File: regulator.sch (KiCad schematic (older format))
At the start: 21 parts, among them IC1 PIC12F675-I/P, Q1 PN2222A, Q2 2N2907A, Q3 PHP18NQ10T, Q4 PN2222A, U1 LM7805

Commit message: Replace old circuit.
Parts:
- added D5: 1N4007, symbol D
- D2: value D -> 1N4004
- Q1, Q4: symbol Q_NPN_EBC -> Q_NPN_EBC-RESCUE-regulator
- Q2: symbol Q_PNP_EBC -> Q_PNP_EBC-RESCUE-regulator
- Q3: value PHP18NQ10T -> BUK9511-55A (Logic Level); symbol Q_NMOS_GDS -> Q_NMOS_GDS-RESCUE-regulator
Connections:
- net BootStrap: no longer U1.VI
- net Vin(14+): now also D5.2 (A); no longer D2.2 (A)
- net at C1.1, IC1.1 (VDD), U1.VO: now also D2.2 (A)
- new net: D5.1 (K), U1.VI
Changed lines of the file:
@@
 EESchema Schematic File Version 2
+LIBS:regulator-rescue
 LIBS:power
 LIBS:device
@@
 encoding utf-8
 Sheet 1 1
-Title "PWM Regulator v1"
-Date "2015'년' 05'월' 29'일' 금요일"
-Rev "1.2"
+Title "PWM Regulator v2"
+Date "2015-06-18"
+Rev "1.2c"
 Comp ""
 Comment1 ""
@@
 Connection ~ 8950 5000
 $Comp
-L Q_NMOS_GDS Q3
+L Q_NMOS_GDS-RESCUE-regulator Q3
 U 1 1 5563B1A2
 P 6600 3250
-F 0 "Q3" H 6900 3300 50  0000 R CNN
-F 1 "PHP18NQ10T" H 7250 3200 50  0000 R CNN
+F 0 "Q3" V 6850 3500 50  0000 R CNN
+F 1 "BUK9511-55A (Logic Level)" V 7000 3500 50  0000 R CNN
 F 2 "" H 6800 3350 29  0000 C CNN
 F 3 "" H 6600 3250 60  0000 C CNN
@@
 $EndComp
 $Comp
-L Q_NPN_EBC Q1
+L Q_NPN_EBC-RESCUE-regulator Q1
 U 1 1 5563BACB
 P 6200 3850
@@
 $EndComp
 $Comp
-L Q_PNP_EBC Q2
+L Q_PNP_EBC-RESCUE-regulator Q2
 U 1 1 5563BB02
 P 6200 4300
@@
 P 4900 3350
 F 0 "D2" H 4900 3450 50  0000 C CNN
-F 1 "D" H 4900 3250 50  0000 C CNN
+F 1 "1N4004" H 4900 3250 50  0000 C CNN
 F 2 "" H 4900 3350 60  0000 C CNN
 F 3 "" H 4900 3350 60  0000 C CNN
@@
 	4650 4150 5250 4150
 Wire Wire Line
-	4750 3350 4600 3350
-Wire Wire Line
-	4600 3350 4600 3150
-Wire Wire Line
 	5250 4150 5250 4400
 $Comp
-L Q_NPN_EBC Q4
+L Q_NPN_EBC-RESCUE-regulator Q4
 U 1 1 55642E1A
 P 5350 4050
@@
 Connection ~ 5450 3750
 Wire Wire Line
-	5450 4250 5450 5000
+	5450 5000 5450 4250
 Connection ~ 5450 5000
 Wire Wire Line
@@
 	2150 5000 9500 5000
 Wire Wire Line
-	2700 4300 2700 4050
+	2700 3350 2700 4300
 Connection ~ 2700 4050
 Wire Wire Line
@@
 $EndComp
 Wire Wire Line
-	7600 3150 7350 3150
-Wire Wire Line
-	7050 3150 6800 3150
-Wire Wire Line
-	5200 3350 5200 3600
-Wire Wire Line
-	5200 3600 1750 3600
-Connection ~ 5200 3350
-Wire Wire Line
-	1750 3600 1750 4050
-Wire Wire Line
-	4600 3150 6400 3150
+	7350 3150 7600 3150
+Wire Wire Line
+	6800 3150 7050 3150
+Wire Wire Line
+	1750 3150 1750 4050
 Text GLabel 2150 2800 0    60   Input ~ 0
 Vin(14+)
@@
 Vin-
 Wire Wire Line
-	2150 5050 1950 5050
+	2150 5050 1900 5050
 Connection ~ 2150 5000
 $Comp
@@
 	5050 4950 5050 5000
 Connection ~ 5050 5000
+Wire Wire Line
+	2700 3350 4750 3350
+Wire Wire Line
+	3500 3150 6400 3150
+$Comp
+L D D5
+U 1 1 558499A4
+P 3350 3150
+F 0 "D5" H 3350 3250 50  0000 C CNN
+F 1 "1N4007" H 3350 3050 50  0000 C CNN
+F 2 "" H 3350 3150 60  0000 C CNN
+F 3 "" H 3350 3150 60  0000 C CNN
+	1    3350 3150
+	1    0    0    1
+$EndComp
+Wire Wire Line
+	3200 3150 1750 3150
 $EndSCHEMATC

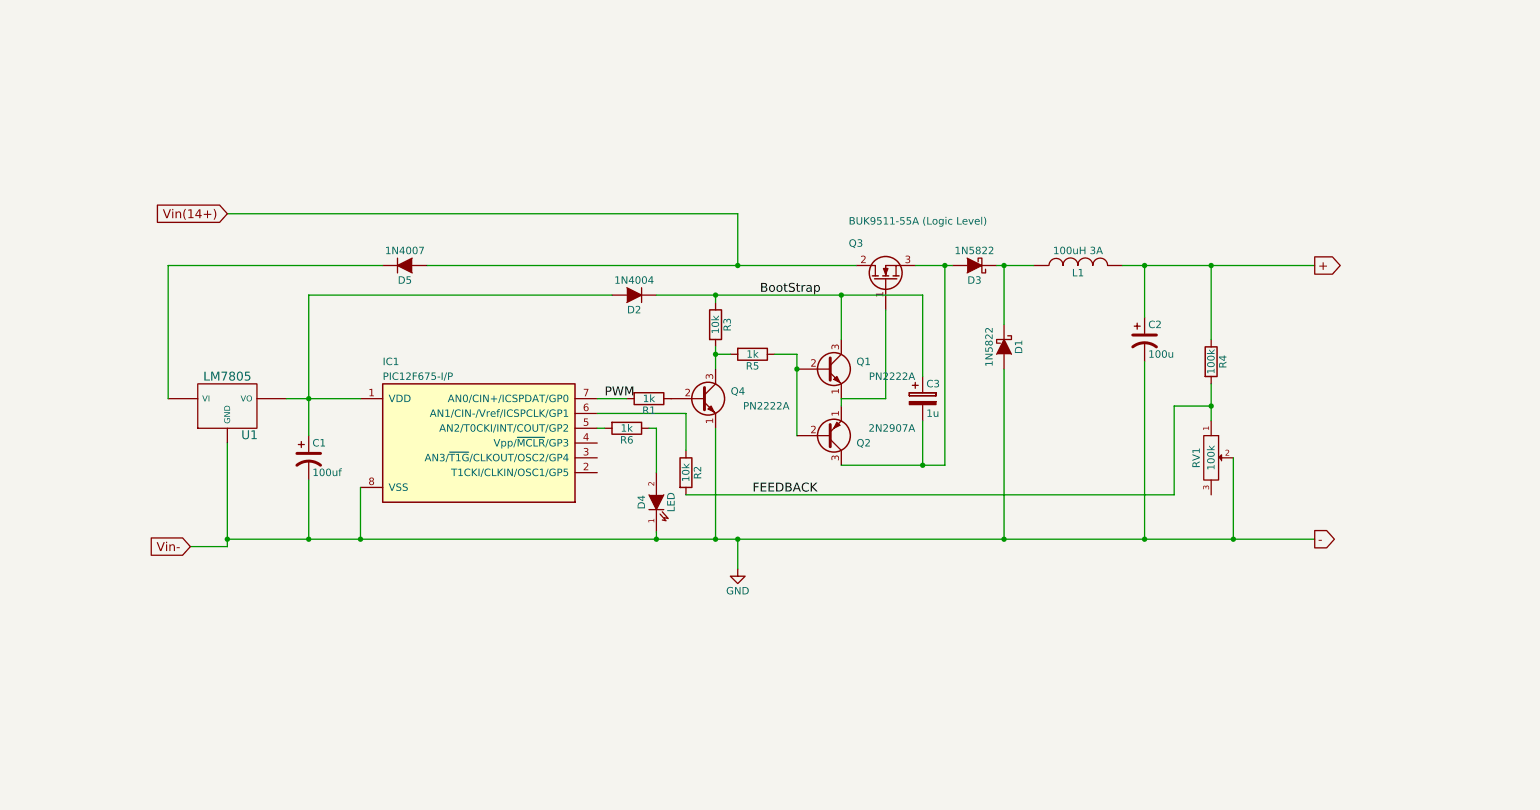
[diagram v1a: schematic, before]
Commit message: Add Solar Engine. It prevent drop PV voltage at low voltage load. It's not fully tested and some noise from switching.
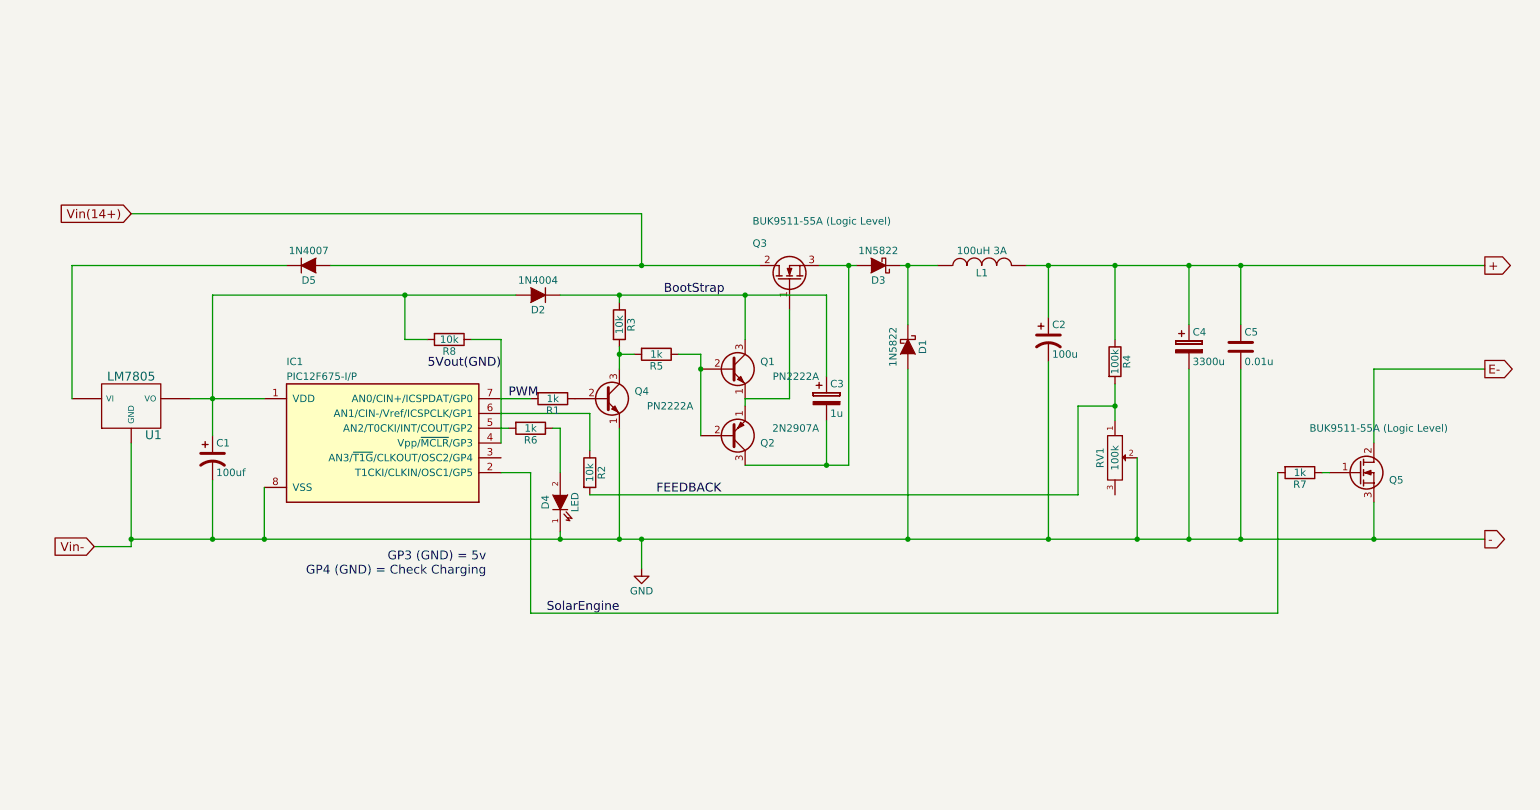
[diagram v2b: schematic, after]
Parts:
- added C4: 3300u, symbol CP
- added C5: 0.01u, symbol C
- added Q5: BUK9511-55A (Logic Level), symbol Q_NMOS_GDS-RESCUE-regulator
- added R7: 1k, symbol R
- added R8: 10k, symbol R
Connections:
- net +: now also C4.1, C5.1
- net GND: now also C4.2, C5.2, Q5.3 (S)
- net at C1.1, D2.2 (A), IC1.1 (VDD)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: now also R8.2
- net SolarEngine: now reaches IC1.2 (T1CKI/CLKIN/OSC1/GP5)
- net SolarEngine: now also R7.2
- net 5Vout(GND): now reaches IC1.4 (Vpp/~MCLR~/GP3)
- net 5Vout(GND): now also R8.1
- new net: Q5.1 (G), R7.1
- new net E-: Q5.2 (D)
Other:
- note added: "GP3 (GND) = 5v\nGP4 (GND) = Check Charging"
- moved on the sheet: C1, C2, C3, D1, D2, D3, D4, D5, IC1, L1, Q1, Q2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

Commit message: Solar Engine is not good idea but test works.
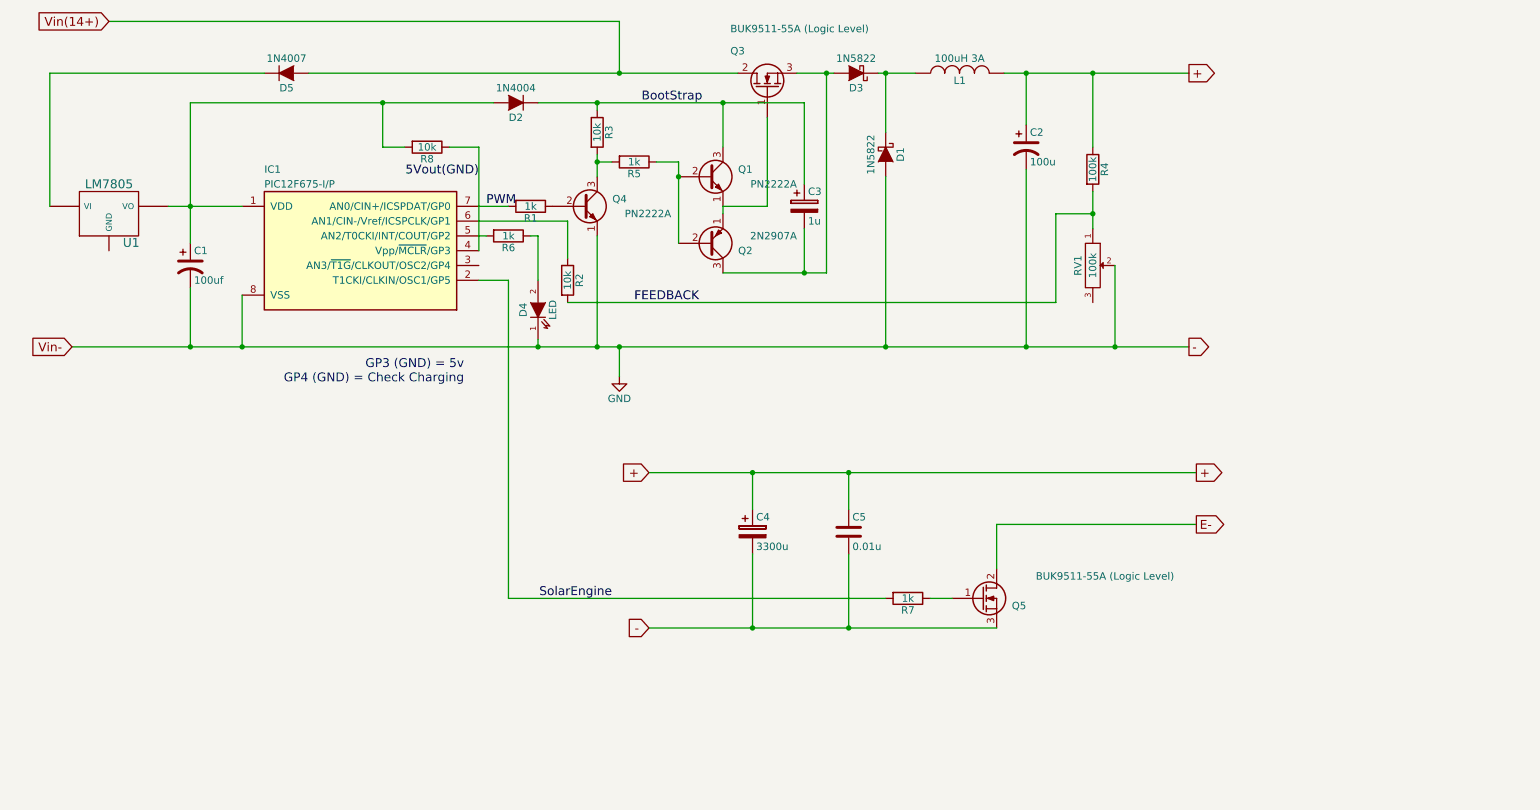
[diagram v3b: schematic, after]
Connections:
- net GND: no longer U1.GND
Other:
- moved on the sheet: C1, C2, C3, C4, C5, D1, D2, D3, D4, D5, IC1, L1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

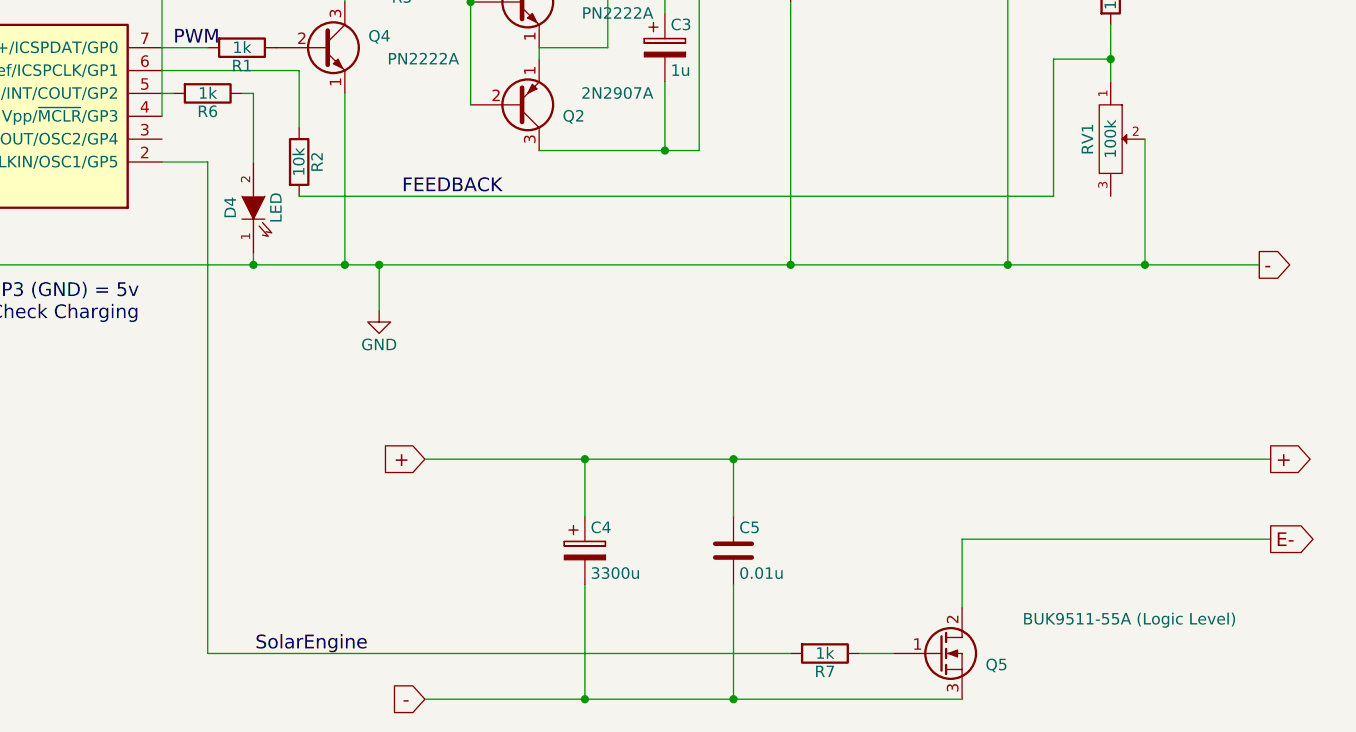
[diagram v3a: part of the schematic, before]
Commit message: Remove Solar Engine. It is useless. Add signal for PWM Sync.
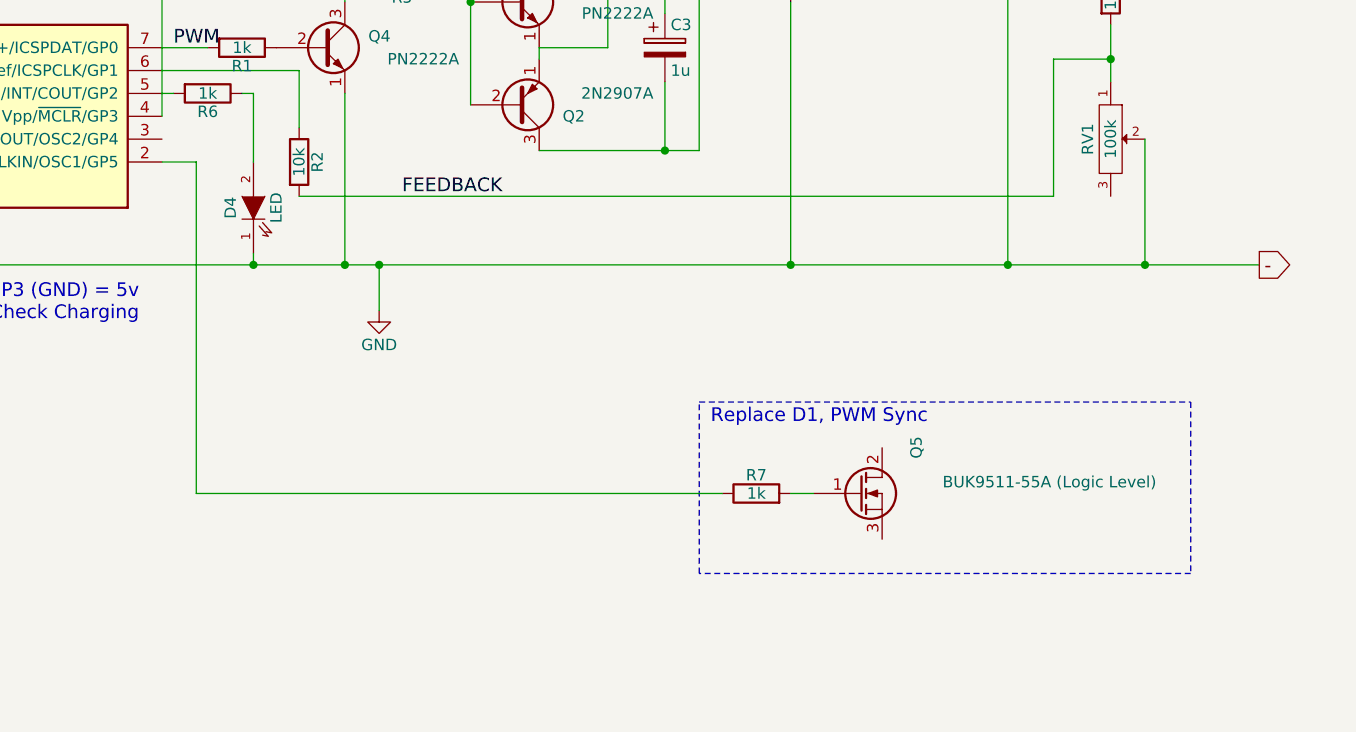
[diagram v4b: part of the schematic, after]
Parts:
- removed C4: 3300u, symbol CP
- removed C5: 0.01u, symbol C
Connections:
- net GND: no longer Q5.3 (S)
- net at R7.1: now also IC1.2 (T1CKI/CLKIN/OSC1/GP5); no longer Q5.1 (G)
- net E-: no longer names the net of Q5.2 (D)
- net SolarEngine: no longer names the net of R7.2
- net SolarEngine: now also Q5.1 (G); no longer IC1.2 (T1CKI/CLKIN/OSC1/GP5)
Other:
- note added: "Replace D1, PWM Sync"
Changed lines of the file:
@@
 Sheet 1 1
 Title "PWM Regulator v3"
-Date "2015-07-14"
-Rev "1.2f"
+Date "2015-07-18"
+Rev "1.2g"
 Comp ""
 Comment1 ""
@@
 $EndComp
 $Comp
-L CP C4
-U 1 1 559FC9C7
-P 5700 4950
-F 0 "C4" H 5725 5050 50  0000 L CNN
-F 1 "3300u" H 5725 4850 50  0000 L CNN
-F 2 "" H 5738 4800 30  0000 C CNN
-F 3 "" H 5700 4950 60  0000 C CNN
-	1    5700 4950
-	1    0    0    -1
-$EndComp
-$Comp
-L C C5
-U 1 1 559FCBD8
-P 6350 4950
-F 0 "C5" H 6375 5050 50  0000 L CNN
-F 1 "0.01u" H 6375 4850 50  0000 L CNN
-F 2 "" H 6388 4800 30  0000 C CNN
-F 3 "" H 6350 4950 60  0000 C CNN
-	1    6350 4950
-	1    0    0    -1
-$EndComp
-$Comp
-L Q_NMOS_GDS-RESCUE-regulator Q5
-U 1 1 559FCD3F
-P 7250 5400
-F 0 "Q5" H 7550 5350 50  0000 R CNN
-F 1 "BUK9511-55A (Logic Level)" H 8550 5550 50  0000 R CNN
-F 2 "" H 7450 5500 29  0000 C CNN
-F 3 "" H 7250 5400 60  0000 C CNN
-	1    7250 5400
-	1    0    0    -1
-$EndComp
-$Comp
-L R R7
-U 1 1 559FD8A6
-P 6750 5400
-F 0 "R7" V 6830 5400 50  0000 C CNN
-F 1 "1k" V 6750 5400 50  0000 C CNN
-F 2 "" V 6680 5400 30  0000 C CNN
-F 3 "" H 6750 5400 30  0000 C CNN
-	1    6750 5400
-	0    1    1    0
-$EndComp
-Text GLabel 8700 4900 2    60   Output ~ 0
-E-
-$Comp
 L R R8
 U 1 1 55A0233C
@@
 Text Label 3850 2550 2    60   ~ 0
 5Vout(GND)
-Text Label 4750 5400 2    60   ~ 0
-SolarEngine
 Text Notes 3750 3950 2    60   ~ 0
 GP3 (GND) = 5v\nGP4 (GND) = Check Charging
-Text GLabel 5000 5600 0    60   Input ~ 0
--
-Text GLabel 8700 4550 2    60   Output ~ 0
-+
-Text GLabel 5000 4550 0    60   Input ~ 0
-+
 Wire Wire Line
 	4800 3700 4800 3900
@@
 Connection ~ 3200 2050
 Wire Wire Line
-	3850 3250 4050 3250
-Wire Wire Line
-	4050 3250 4050 5400
-Wire Wire Line
-	7350 5200 7350 4900
-Wire Wire Line
-	7350 4900 8700 4900
-Wire Wire Line
-	6900 5400 7050 5400
-Wire Wire Line
-	5000 4550 8700 4550
-Wire Wire Line
-	5000 5600 7350 5600
-Wire Wire Line
-	5700 5100 5700 5600
-Connection ~ 5700 5600
-Wire Wire Line
-	5700 4800 5700 4550
-Connection ~ 5700 4550
-Wire Wire Line
-	6350 5100 6350 5600
-Connection ~ 6350 5600
-Wire Wire Line
-	6350 4800 6350 4550
-Connection ~ 6350 4550
-Wire Wire Line
-	4050 5400 6600 5400
+	3850 3250 4000 3250
+$Comp
+L R R7
+U 1 1 55A9A097
+P 6450 4700
+F 0 "R7" V 6530 4700 50  0000 C CNN
+F 1 "1k" V 6450 4700 50  0000 C CNN
+F 2 "" V 6380 4700 30  0000 C CNN
+F 3 "" H 6450 4700 30  0000 C CNN
+	1    6450 4700
+	0    -1   -1   0
+$EndComp
+Wire Wire Line
+	6300 4700 4000 4700
+Wire Wire Line
+	4000 4700 4000 3250
+$Comp
+L Q_NMOS_GDS-RESCUE-regulator Q5
+U 1 1 55A9A277
+P 6900 4700
+F 0 "Q5" V 7150 4950 50  0000 R CNN
+F 1 "BUK9511-55A (Logic Level)" H 8200 4750 50  0000 R CNN
+F 2 "" H 7100 4800 29  0000 C CNN
+F 3 "" H 6900 4700 60  0000 C CNN
+	1    6900 4700
+	1    0    0    -1
+$EndComp
+Wire Wire Line
+	6700 4700 6600 4700
+Wire Notes Line
+	8350 4300 8350 5050
+Wire Notes Line
+	8350 5050 6200 5050
+Wire Notes Line
+	6200 5050 6200 4300
+Wire Notes Line
+	6200 4300 8350 4300
+Text Notes 6250 4400 0    60   ~ 0
+Replace D1, PWM Sync
 $EndSCHEMATC

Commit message: Schematic update. capacitor to 220uF.
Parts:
- C2: value 100u -> 220u(or Higher)
- L1: value 100uH 3A -> 100uH 3A (or Higher)
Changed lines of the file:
@@
 Sheet 1 1
 Title "PWM Regulator v3"
-Date "2015-07-18"
-Rev "1.2g"
+Date "2015-07-25"
+Rev "1.2h"
 Comp ""
 Comment1 ""
@@
 P 7100 1850
 F 0 "L1" V 7050 1850 50  0000 C CNN
-F 1 "100uH 3A" V 7200 1850 50  0000 C CNN
+F 1 "100uH 3A (or Higher)" V 7200 1850 50  0000 C CNN
 F 2 "" H 7100 1850 60  0000 C CNN
 F 3 "" H 7100 1850 60  0000 C CNN
@@
 P 7550 2350
 F 0 "C2" H 7575 2450 50  0000 L CNN
-F 1 "100u" H 7575 2250 50  0000 L CNN
+F 1 "220u(or Higher)" H 6900 2150 50  0000 L CNN
 F 2 "" H 7550 2350 60  0000 C CNN
 F 3 "" H 7550 2350 60  0000 C CNN

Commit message: Use more big capacitor and more current output. 470uF is good for 2A or higher output.
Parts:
- C2: value 220u(or Higher) -> 420u(or Higher, 470uF also good)
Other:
- note added: "Output 2A -> C2 > 420uF"
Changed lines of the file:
@@
 Sheet 1 1
 Title "PWM Regulator v3"
-Date "2015-07-25"
-Rev "1.2h"
+Date "2015-07-27"
+Rev "1.2i"
 Comp ""
 Comment1 ""
@@
 P 7550 2350
 F 0 "C2" H 7575 2450 50  0000 L CNN
-F 1 "220u(or Higher)" H 6900 2150 50  0000 L CNN
+F 1 "420u(or Higher, 470uF also good)" H 6950 2000 50  0000 L CNN
 F 2 "" H 7550 2350 60  0000 C CNN
 F 3 "" H 7550 2350 60  0000 C CNN
@@
 Text Notes 6250 4400 0    60   ~ 0
 Replace D1, PWM Sync
+Text Notes 2600 4250 0    60   ~ 0
+Output 2A -> C2 > 420uF
 $EndSCHEMATC

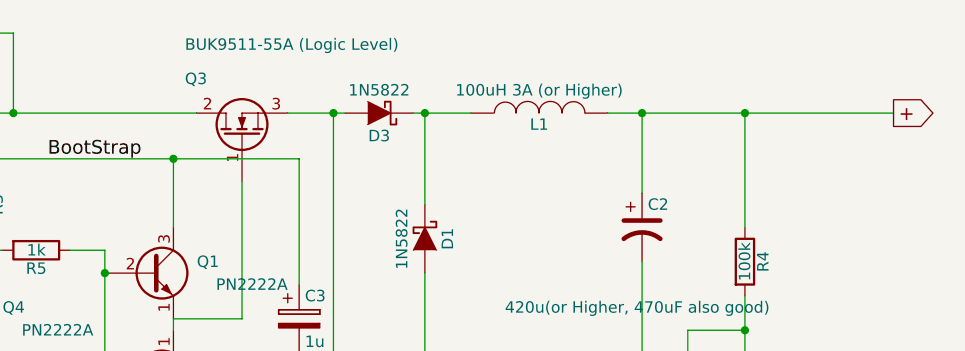
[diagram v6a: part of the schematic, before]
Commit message: Inductor to 330uH. This is good at low frequency.
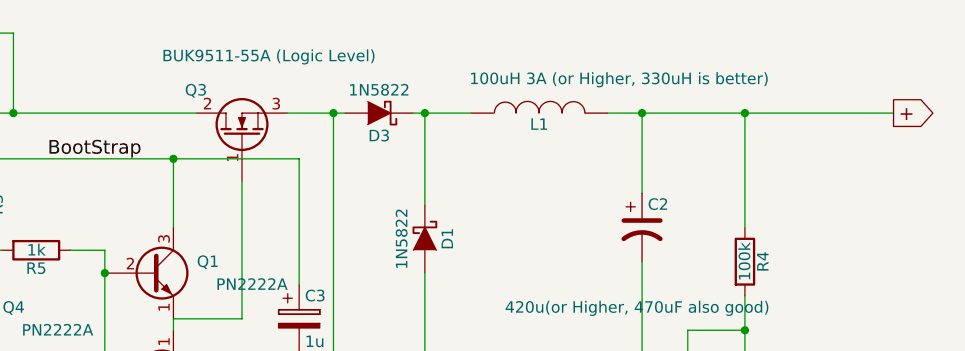
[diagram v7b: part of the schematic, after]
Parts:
- L1: value 100uH 3A (or Higher) -> 100uH 3A (or Higher, 330uH is better)
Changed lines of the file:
@@
 Sheet 1 1
 Title "PWM Regulator v3"
-Date "2015-07-27"
-Rev "1.2i"
+Date "2015-07-30"
+Rev "1.2j"
 Comp ""
 Comment1 ""
@@
 P 7100 1850
 F 0 "L1" V 7050 1850 50  0000 C CNN
-F 1 "100uH 3A (or Higher)" V 7200 1850 50  0000 C CNN
+F 1 "100uH 3A (or Higher, 330uH is better)" V 7250 1500 50  0000 C CNN
 F 2 "" H 7100 1850 60  0000 C CNN
 F 3 "" H 7100 1850 60  0000 C CNN
@@
 U 1 1 5563B1A2
 P 5800 1950
-F 0 "Q3" V 6050 2200 50  0000 R CNN
-F 1 "BUK9511-55A (Logic Level)" V 6200 2200 50  0000 R CNN
+F 0 "Q3" V 6000 2200 50  0000 R CNN
+F 1 "BUK9511-55A (Logic Level)" V 6150 2300 50  0000 R CNN
 F 2 "" H 6000 2050 29  0000 C CNN
 F 3 "" H 5800 1950 60  0000 C CNN
